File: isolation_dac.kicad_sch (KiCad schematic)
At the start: 29 parts, among them IC1 DAC63204RTERQ1, IC2 ISO7640FMDWR, IC5 REF35409QDBVR, J4 Conn_01x03, J6 Conn_02x04_Odd_Even, T1 760390015, U3 TPS76350DBVRG4

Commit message: feat: adding goochain jack 2.35 mm to design
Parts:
- C18, C21, C22, C24, C26, C29: S1P# (none) -> 187-CL21B104KBCNNND
- C19: footprint Capacitor_Tantalum_SMD:CP_EIA-2012-12_Kemet-R_Pad1.30x1.05mm_HandSolder -> Capacitor_SMD:C_0805_2012Metric_Pad1.18x1.45mm_HandSolder; MFN Vishay / Sprague -> TAIYO YUDEN; MFP TMCP1A475KTR2F -> TMK212AB7475KG-T; S1P# (none) -> 963-TMK212AB7475KG-T; S1PL https://eu.mouser.com/ProductDetail/Vishay-Sprague/TMCP1A47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 -> https://eu.mouser.com/ProductDetail/TAIYO-YUDEN/TMK212AB747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
- C20: S1P# (none) -> 187-CL21A106KOQNNNE
- C23, C25, C27: S1P# (none) -> 187-CL21B105KAFNNNF
- C28: MFN Vishay / Sprague -> KEMET; MFP TMCP1D155KTR2F -> C0805C155K4RECTU; S1P# (none) -> 80-C0805C155K4RECTU; S1PL https://eu.mouser.com/ProductDetail/Vishay-Sprague/TMCP1D15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 -> https://eu.mouser.com/ProductDetail/KEMET/C0805C155K4RECTU?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
- C30: S1P# (none) -> 755-TCSP1D106M8R
- D7, D8: S1P# (none) -> 833-MBR0520-TP
- IC1: MFN (none) -> Texas Instruments; MFP (none) -> DAC63204RTERQ1; S1P# (none) -> 595-DAC63204RTERQ1; S1PL (none) -> https://eu.mouser.com/ProductDetail/Texas-Instruments/DAC63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; S1PN (none) -> Mouser
- IC2: S1P# (none) -> 595-ISO7640FMDWR
- IC5: S1P# (none) -> 595-REF35409QDBVR
- J4: S1P# (none) -> 523-G800W305018EU
- J6: S1P# (none) -> 200-TSW10207TD
- PS2: S1P# (none) -> 595-SN6501DBVR
- R6, R7: S1P# (none) -> 603-RC0805FR-103K32L
- T1: S1P# (none) -> 710-760390015
- U3: S1P# (none) -> 595-TPS76350DBVRG4

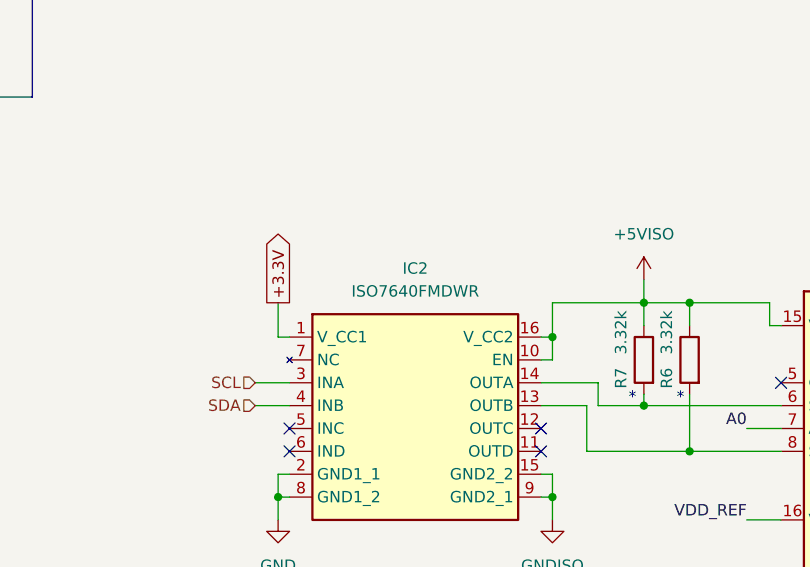
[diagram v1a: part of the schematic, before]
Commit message: docs: update BOM
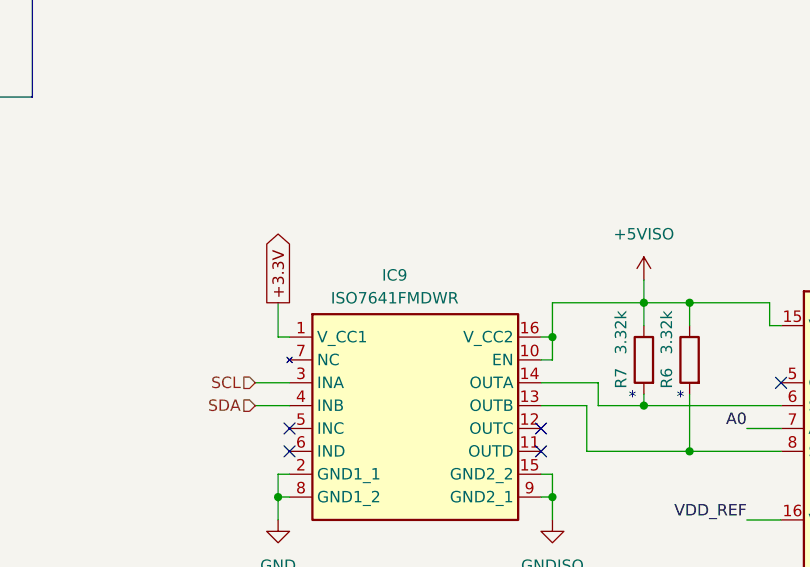
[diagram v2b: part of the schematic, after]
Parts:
- removed IC2: ISO7640FMDWR, Package_SO:SOIC-16W_7.5x10.3mm_P1.27mm, symbol Technaid:ISO7640FMDWR
- added IC9: ISO7641FMDWR, Package_SO:SOIC-16W_7.5x10.3mm_P1.27mm, symbol Technaid:ISO7640FMDWR
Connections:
- net +3.3V: now also IC9.1 (V_CC1)
- net +5VISO: now also IC9.10 (EN), IC9.16 (V_CC2)
- net GND: now also IC9.2 (GND1_1), IC9.8 (GND1_2)
- net GNDISO: now also IC9.15 (GND2_2), IC9.9 (GND2_1)
- net SCL: now also IC9.3 (INA)
- net SDA: now also IC9.4 (INB)
- net at IC1.8 (SDA/SCLK), R6.2: now also IC9.13 (OUTB)
- net at IC1.6 (SCL/~{SYNC}), R7.2: now also IC9.14 (OUTA)
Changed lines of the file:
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@@
 	)
 	(symbol
-		(lib_id "Technaid:ISO7640FMDWR")
-		(at 100.33 102.87 0)
-		(unit 1)
-		(exclude_from_sim no)
-		(in_bom yes)
-		(on_board yes)
-		(dnp no)
-		(fields_autoplaced yes)
-		(property "Reference" "IC2"
-			(at 116.84 95.25 0)
-			(effects
-				(font
-					(size 1.27 1.27)
-				)
-			)
-		)
-		(property "Value" "ISO7640FMDWR"
-			(at 116.84 97.79 0)
-			(effects
-				(font
-					(size 1.27 1.27)
-				)
-			)
-		)
-		(property "Footprint" "Package_SO:SOIC-16W_7.5x10.3mm_P1.27mm"
-			(at 129.54 197.79 0)
-			(effects
-				(font
-					(size 1.27 1.27)
-				)
-				(justify left top)
-				(hide yes)
-			)
-		)
-		(property "Datasheet" "http://www.ti.com/lit/gpn/ISO7640FM"
-			(at 129.54 297.79 0)
-			(effects
-				(font
-					(size 1.27 1.27)
-				)
-				(justify left top)
-				(hide yes)
-			)
-		)
-		(property "Description" "6kVpk Low Power Quad Channels, 150Mbps Digital Isolators"
-			(at 100.33 102.87 0)
-			(effects
-				(font
-					(size 1.27 1.27)
-				)
-				(hide yes)
-			)
-		)
-		(property "Height" "2.65"
-			(at 129.54 497.79 0)
-			(effects
-				(font
-					(size 1.27 1.27)
-				)
-				(justify left top)
-				(hide yes)
-			)
-		)
-		(property "Mouser Part Number" "595-ISO7640FMDWR"
-			(at 129.54 597.79 0)
-			(effects
-				(font
-					(size 1.27 1.27)
-				)
-				(justify left top)
-				(hide yes)
-			)
-		)
-		(property "Mouser Price/Stock" "https://www.mouser.co.uk/ProductDetail/Texas-Instruments/ISO7640FMDWR?qs=bhx7MkwkKU8Q7CcjCV9mvg%3D%3D"
-			(at 129.54 697.79 0)
-			(effects
-				(font
-					(size 1.27 1.27)
-				)
-				(justify left top)
-				(hide yes)
-			)
-		)
-		(property "Manufacturer_Name" "Texas Instruments"
-			(at 129.54 797.79 0)
-			(effects
-				(font
-					(size 1.27 1.27)
-				)
-				(justify left top)
-				(hide yes)
-			)
-		)
-		(property "Manufacturer_Part_Number" "ISO7640FMDWR"
-			(at 129.54 897.79 0)
-			(effects
-				(font
-					(size 1.27 1.27)
-				)
-				(justify left top)
-				(hide yes)
-			)
-		)
-		(property "MFN" "Texas Instruments"
-			(at 100.33 102.87 0)
-			(effects
-				(font
-					(size 1.27 1.27)
-				)
-				(hide yes)
-			)
-		)
-		(property "MFP" "ISO7640FMDWR"
-			(at 100.33 102.87 0)
-			(effects
-				(font
-					(size 1.27 1.27)
-				)
-				(hide yes)
-			)
-		)
-		(property "S1PN" "Mouser"
-			(at 100.33 102.87 0)
-			(effects
-				(font
-					(size 1.27 1.27)
-				)
-				(hide yes)
-			)
-		)
-		(property "S1PL" "https://www.mouser.co.uk/ProductDetail/Texas-Instruments/ISO7640FMDWR?qs=bhx7MkwkKU8Q7CcjCV9mvg%3D%3D"
-			(at 100.33 102.87 0)
-			(effects
-				(font
-					(size 1.27 1.27)
-				)
-				(hide yes)
-			)
-		)
-		(property "S1P#" "595-ISO7640FMDWR"
-			(at 100.33 102.87 0)
-			(effects
-				(font
-					(size 1.27 1.27)
-				)
-				(hide yes)
-			)
-		)
-		(pin "16"
-		)
-		(pin "10"
-		)
-		(pin "15"
-		)
-		(pin "13"
-		)
-		(pin "6"
-		)
-		(pin "14"
-		)
-		(pin "2"
-		)
-		(pin "12"
-		)
-		(pin "4"
-		)
-		(pin "7"
-		)
-		(pin "11"
-		)
-		(pin "9"
-		)
-		(pin "3"
-		)
-		(pin "8"
-		)
-		(pin "1"
-		)
-		(pin "5"
-		)
-		(instances
-			(project "techstim-hardware"
-				(path "/1d5ae591-53a2-4652-87aa-0cddc0836341/6f1c9813-6d9b-43a0-a5d7-e66a0b6ca03e"
-					(reference "IC2")
-					(unit 1)
-				)
-			)
-		)
-	)
-	(symbol
 		(lib_id "Device:C")
 		(at 57.15 62.23 0)
@@
 					(unit 1)
 				)
+			)
+		)
+	)
+	(symbol
+		(lib_id "Technaid:ISO7640FMDWR")
+		(at 100.33 102.87 0)
+		(unit 1)
+		(exclude_from_sim no)
+		(in_bom yes)
+		(on_board yes)
+		(dnp no)
+		(property "Reference" "IC9"
+			(at 114.554 96.012 0)
+			(effects
+				(font
+					(size 1.27 1.27)
+				)
+			)
+		)
+		(property "Value" "ISO7641FMDWR"
+			(at 114.554 98.552 0)
+			(effects
+				(font
+					(size 1.27 1.27)
+				)
+			)
+		)
+		(property "Footprint" "Package_SO:SOIC-16W_7.5x10.3mm_P1.27mm"
+			(at 105.156 123.952 0)
+			(effects
+				(font
+					(size 1.27 1.27)
+				)
+				(justify left top)
+				(hide yes)
+			)
+		)
+		(property "Datasheet" "http://www.ti.com/lit/gpn/ISO7640FM"
+			(at 129.54 297.79 0)
+			(effects
+				(font
+					(size 1.27 1.27)
+				)
+				(justify left top)
+				(hide yes)
+			)
+		)
+		(property "Description" "6kVpk Low Power Quad Channels, 150Mbps Digital Isolators"
+			(at 100.33 102.87 0)
+			(effects
+				(font
+					(size 1.27 1.27)
+				)
+				(hide yes)
+			)
+		)
+		(property "Height" "2.65"
+			(at 129.54 497.79 0)
+			(effects
+				(font
+					(size 1.27 1.27)
+				)
+				(justify left top)
+				(hide yes)
+			)
+		)
+		(property "Mouser Part Number" "595-ISO7640FMDWR"
+			(at 129.54 597.79 0)
+			(effects
+				(font
+					(size 1.27 1.27)
+				)
+				(justify left top)
+				(hide yes)
+			)
+		)
+		(property "Mouser Price/Stock" "https://www.mouser.co.uk/ProductDetail/Texas-Instruments/ISO7640FMDWR?qs=bhx7MkwkKU8Q7CcjCV9mvg%3D%3D"
+			(at 129.54 697.79 0)
+			(effects
+				(font
+					(size 1.27 1.27)
+				)
+				(justify left top)
+				(hide yes)
+			)
+		)
+		(property "Manufacturer_Name" "Texas Instruments"
+			(at 129.54 797.79 0)
+			(effects
+				(font
+					(size 1.27 1.27)
+				)
+				(justify left top)
+				(hide yes)
+			)
+		)
+		(property "Manufacturer_Part_Number" "ISO7640FMDWR"
+			(at 129.54 897.79 0)
+			(effects
+				(font
+					(size 1.27 1.27)
+				)
+				(justify left top)
+				(hide yes)
+			)
+		)
+		(property "MFN" "Texas Instruments"
+			(at 100.33 102.87 0)
+			(effects
+				(font
+					(size 1.27 1.27)
+				)
+				(hide yes)
+			)
+		)
+		(property "MFP" "ISO7640FMDWR"
+			(at 100.33 102.87 0)
+			(effects
+				(font
+					(size 1.27 1.27)
+				)
+				(hide yes)
+			)
+		)
+		(property "S1PN" "Mouser"
+			(at 100.33 102.87 0)
+			(effects
+				(font
+					(size 1.27 1.27)
+				)
+				(hide yes)
+			)
+		)
+		(property "S1PL" "https://www.mouser.co.uk/ProductDetail/Texas-Instruments/ISO7640FMDWR?qs=bhx7MkwkKU8Q7CcjCV9mvg%3D%3D"
+			(at 100.33 102.87 0)
+			(effects
+				(font
+					(size 1.27 1.27)
+				)
+				(hide yes)
+			)
+		)
+		(property "S1P#" "595-ISO7640FMDWR"
+			(at 100.33 102.87 0)
+			(effects
+				(font
+					(size 1.27 1.27)
+				)
+				(hide yes)
+			)
+		)
+		(pin "10"
+		)
+		(pin "4"
+		)
+		(pin "8"
+		)
+		(pin "6"
+		)
+		(pin "7"
+		)
+		(pin "2"
+		)
+		(pin "1"
+		)
+		(pin "13"
+		)
+		(pin "15"
+		)
+		(pin "16"
+		)
+		(pin "14"
+		)
+		(pin "11"
+		)
+		(pin "12"
+		)
+		(pin "3"
+		)
+		(pin "5"
+		)
+		(pin "9"
+		)
+		(instances
+			(project "techstim-hardware"
+				(path "/1d5ae591-53a2-4652-87aa-0cddc0836341/6f1c9813-6d9b-43a0-a5d7-e66a0b6ca03e"
+					(reference "IC9")
+					(unit 1)
+				)

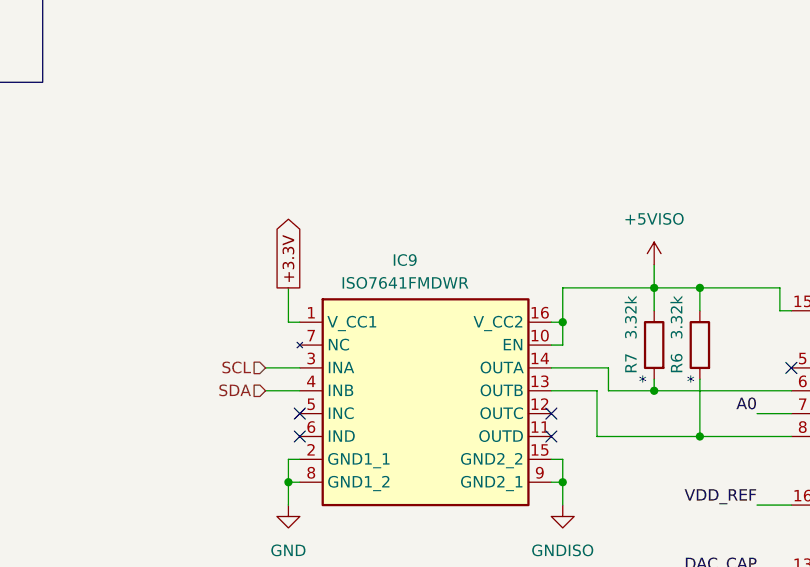
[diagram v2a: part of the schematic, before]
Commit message: fix: update names for IC components
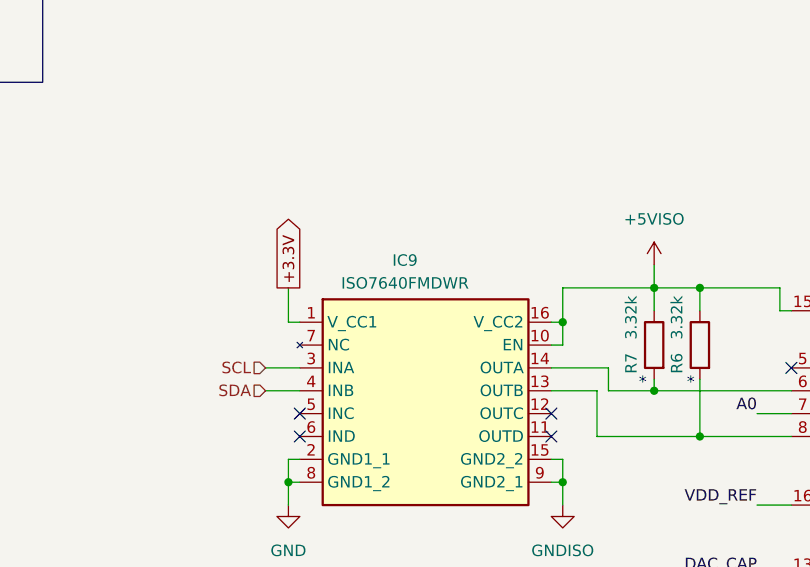
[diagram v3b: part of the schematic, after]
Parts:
- IC9: value ISO7641FMDWR -> ISO7640FMDWR
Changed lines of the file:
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@@
 			)
 		)
-		(property "Value" "ISO7641FMDWR"
+		(property "Value" "ISO7640FMDWR"
 			(at 114.554 98.552 0)
 			(effects
